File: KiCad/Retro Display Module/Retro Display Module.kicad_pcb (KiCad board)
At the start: 2 copper layers, 70 x 100 mm, 114 parts, among them J1 Conn_01x04_Pin, J10 Conn_01x02_Pin, J11 Conn_01x02_Pin, J12 VCC, J13 TX, J14 RX, J15 CFG, J16 SEL, J17 GND, J18 Conn_01x04_Pin, J19 Conn_01x04_Pin, J2 VCC, J20 Conn_01x02_Pin, J21 Conn_01x04_Pin, J22 Conn_01x02_Pin, J23 Conn_01x02_Pin, J24 Conn_01x02_Pin, J25 Conn_02x03_Odd_Even, J26 Conn_01x02_Pin, J27 Conn_01x02_Pin, J28 Conn_01x02_Pin, J29 Conn_01x04_Pin, J3 TX, J30 Conn_01x02_Pin, J31 Conn_01x02_Pin, J32 Conn_02x11_Odd_Even, J4 RX, J5 CFG, J6 SEL, J7 GND, J8 Conn_01x02_Pin, J9 Conn_01x02_Pin, U1 TS-1187A-B-A-B, U10 D882_C9634, U11 OP07CDR, U12 D882_C9634, U13 D882_C9634, U14 D882_C9634, U15 D882_C9634, U16 D882_C9634, U17 D882_C9634, U18 D882_C9634, U2 STM32G030C8T6, U3 AO3401A, U4 TPS5430DDAR, U5 XC6206P332MR, U6 2N7002, U7 D882_C9634, U8 D882_C9634, U9 D882_C9634, Y1 Crystal

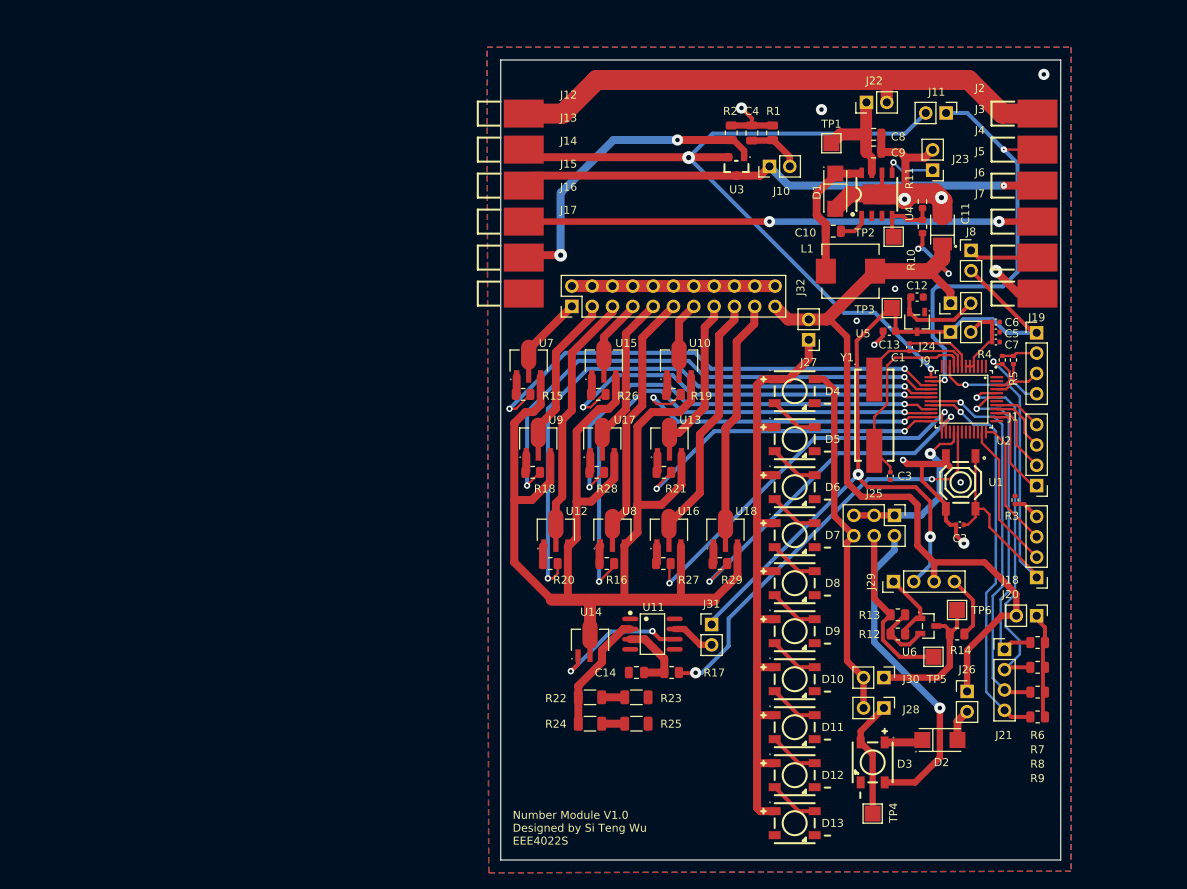
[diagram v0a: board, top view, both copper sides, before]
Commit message: Updated USB PD and Driver LED circuit
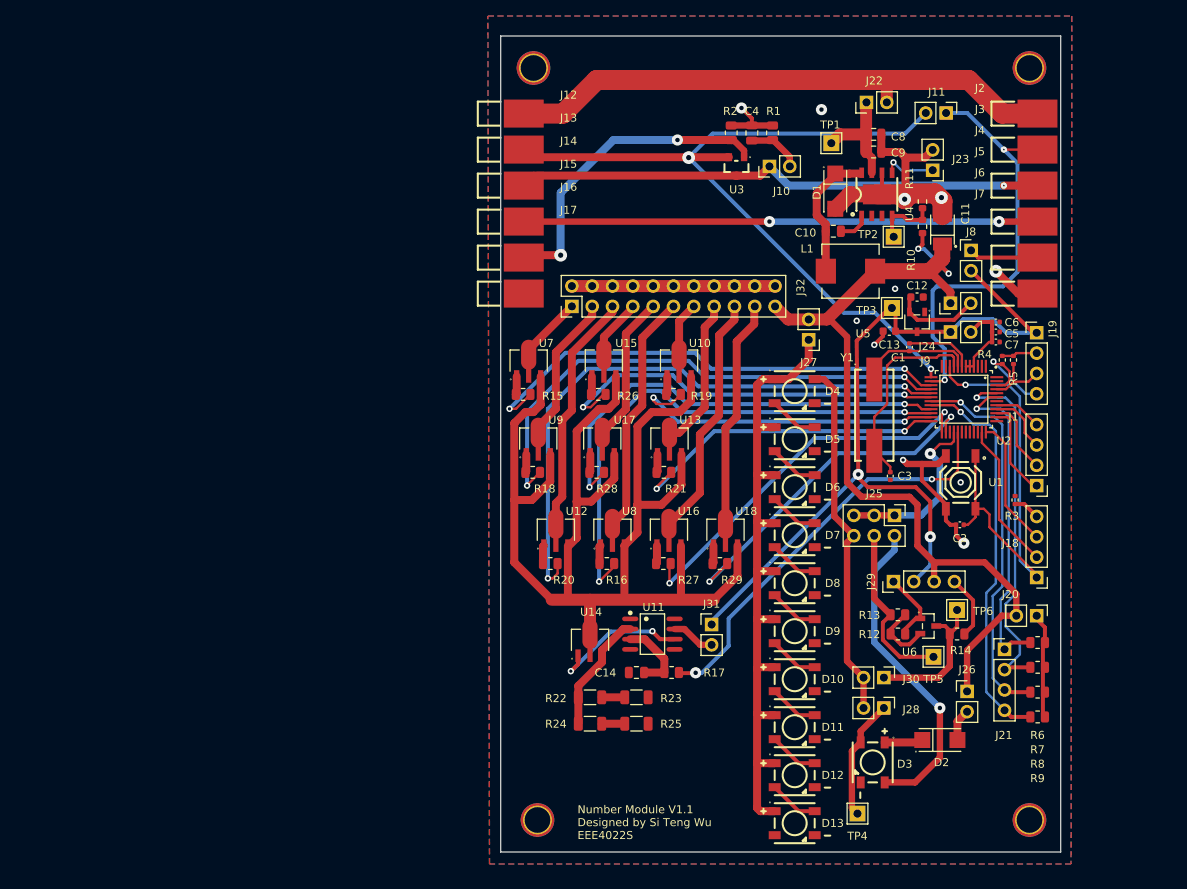
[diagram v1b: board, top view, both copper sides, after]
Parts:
- added H1: M3, Library:MountingHole_3.2mm_M3_Pad_TopBottom, F.Cu at (120.0, 47.0)
- added H2: M3, Library:MountingHole_3.2mm_M3_Pad_TopBottom, F.Cu at (182.0, 47.0)
- added H3: M3, Library:MountingHole_3.2mm_M3_Pad_TopBottom, F.Cu at (120.5, 141.0)
- added H4: M3, Library:MountingHole_3.2mm_M3_Pad_TopBottom, F.Cu at (182.0, 141.0)
- TP1, TP2, TP3, TP4, TP5, TP6: footprint TestPoint:TestPoint_Pad_2.0x2.0mm -> Library:TestPoint_THTPad_2.0x2.0mm_Drill1.0mm
- moved TP4 1.90 mm to (160.5, 140.2)
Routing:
- net GND: track 86.6 -> 85.6 mm, vias 12 -> 11
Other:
- board size 70 x 100 mm -> 70 x 102 mm
- board text added: "Number Module V1.1 Designed by Si Teng Wu EEE4022S"
- board text removed: "Number Module V1.0 Designed by Si Teng Wu EEE4022S"

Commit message: Updated Display PCB
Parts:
- added J33: Conn_01x02_Pin, Connector_PinHeader_2.54mm:PinHeader_1x02_P2.54mm_Vertical, F.Cu at (93.5, 107.2)
- added J34: Conn_02x04_Odd_Even, Connector_PinHeader_2.54mm:PinHeader_2x04_P2.54mm_Vertical, F.Cu at (80.7, 98.9)
- added R30: 100k, Resistor_SMD:R_0402_1005Metric, F.Cu at (85.6, 87.6)
- added R31: 1k, Resistor_SMD:R_0402_1005Metric, F.Cu at (85.6, 89.6)
- added R32: 100k, Resistor_SMD:R_0402_1005Metric, F.Cu at (85.6, 91.6)
- added R33: 1k, Resistor_SMD:R_0402_1005Metric, F.Cu at (85.6, 93.6)
- added R34: 100k, Resistor_SMD:R_0402_1005Metric, F.Cu at (85.6, 95.5)
- added R35: 1k, Resistor_SMD:R_0402_1005Metric, F.Cu at (88.5, 87.6)
- added R36: 100k, Resistor_SMD:R_0402_1005Metric, F.Cu at (88.5, 89.6)
- added R37: 1k, Resistor_SMD:R_0402_1005Metric, F.Cu at (88.5, 91.6)
- added R38: 100k, Resistor_SMD:R_0402_1005Metric, F.Cu at (88.5, 93.6)
- added R39: 1k, Resistor_SMD:R_0402_1005Metric, F.Cu at (88.5, 95.5)
- added R40: 100, Resistor_SMD:R_1206_3216Metric, F.Cu at (88.4, 108.1)
- added R41: 100k, Resistor_SMD:R_0402_1005Metric, F.Cu at (63.6, 101.8)
- added R42: 1k, Resistor_SMD:R_0402_1005Metric, F.Cu at (63.6, 103.8)
- added R43: 100k, Resistor_SMD:R_0402_1005Metric, F.Cu at (63.6, 105.7)
- added R44: 1k, Resistor_SMD:R_0402_1005Metric, F.Cu at (63.6, 107.7)
- added TP7: TestPoint, Library:TestPoint_THTPad_2.0x2.0mm_Drill1.0mm, F.Cu at (80.4, 110.8)
- added U19: AO3401A, Library:SOT-23_L2.9-W1.3-P1.90-LS2.4-BR, F.Cu at (57.1, 88.7)
- added U20: AO3401A, Library:SOT-23_L2.9-W1.3-P1.90-LS2.4-BR, F.Cu at (57.1, 93.4)
- added U21: AO3401A, Library:SOT-23_L2.9-W1.3-P1.90-LS2.4-BR, F.Cu at (57.1, 98.2)
- C14: value 22uF -> 0.1uF; footprint Capacitor_SMD:C_0805_2012Metric -> Capacitor_SMD:C_0402_1005Metric
- C4: value 1nF -> 1uF; footprint Capacitor_SMD:C_0805_2012Metric -> Capacitor_SMD:C_0603_1608Metric
- J1: value Conn_01x04_Pin -> Conn_02x04_Odd_Even; footprint Connector_PinHeader_2.54mm:PinHeader_1x04_P2.54mm_Vertical -> Connector_PinHeader_2.54mm:PinHeader_2x04_P2.54mm_Vertical
- J18, J19: value Conn_01x04_Pin -> Conn_02x03_Odd_Even; footprint Connector_PinHeader_2.54mm:PinHeader_1x04_P2.54mm_Vertical -> Connector_PinHeader_2.54mm:PinHeader_2x03_P2.54mm_Vertical
- J31: value Conn_01x02_Pin -> Conn_01x12_Pin; footprint Connector_PinHeader_2.54mm:PinHeader_1x02_P2.54mm_Vertical -> Connector_PinHeader_2.54mm:PinHeader_1x12_P2.54mm_Vertical
- J32: footprint Connector_PinHeader_2.54mm:PinHeader_2x11_P2.54mm_Vertical -> Connector_PinHeader_2.54mm:PinHeader_2x10_P2.54mm_Vertical
- R1: value 4.7k -> 1k
- R15, R18, R20, R26, R28: value 470 -> 100k; footprint Resistor_SMD:R_0805_2012Metric -> Resistor_SMD:R_0402_1005Metric
- R16, R19, R21, R27, R29: value 470 -> 1k; footprint Resistor_SMD:R_0805_2012Metric -> Resistor_SMD:R_0402_1005Metric
- R22, R23, R24, R25: value 10 -> 100
- U10, U12, U13, U15, U16, U17, U7, U8, U9: value D882_C9634 -> AO3401A; footprint Library:D882 -> Library:SOT-23_L2.9-W1.3-P1.90-LS2.4-BR
- U11: value OP07CDR -> AO3401A; footprint Library:SOIC-8_L4.9-W3.9-P1.27-LS6.0-BL -> Library:SOT-23_L2.9-W1.3-P1.90-LS2.4-BR
- U18: value D882_C9634 -> LM358DR2G; footprint Library:D882 -> Library:Dual LM358
- moved J18 125.9 mm to (57.2, 103.1), turned to 0 degrees
- moved J1 121.3 mm to (62.0, 88.9), turned to 0 degrees
- moved J10 106.6 mm to (57.2, 112.8), turned to 0 degrees
- moved R1 104.9 mm to (61.8, 111.9), turned to 0 degrees
- moved J19 91.0 mm to (92.3, 88.9)
- moved C4 81.8 mm to (87.6, 111.0), turned to 0 degrees
- moved U10 69.7 mm to (71.0, 102.9), turned to 0 degrees
- moved U11 64.7 mm to (71.0, 107.6), turned to 0 degrees
- moved R29 62.0 mm to (82.7, 95.5)
- moved U13 61.2 mm to (75.8, 93.4), turned to 0 degrees
- moved U16 61.2 mm to (75.8, 102.9), turned to 0 degrees
- moved U8 60.0 mm to (71.0, 93.4), turned to 0 degrees
- moved R19 58.0 mm to (79.8, 93.6)
- moved R27 56.3 mm to (82.7, 91.6)
- moved U15 54.8 mm to (75.8, 98.2), turned to 0 degrees
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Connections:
- C14 pad 1: Net-(U11-IN+) -> Net-(J34-Pin_1)
- C4 pad 1: Net-(J10-Pin_2) -> Net-(J19-Pin_5)
- J1 pad 1: Net-(J1-Pin_1) -> /PC6
- J1 pad 3: Net-(J1-Pin_3) -> /PC7
- J14 pad 1: Net-(J10-Pin_1) -> Net-(J14-Pin_1)
- J18 pad 1: /NRST -> /5V
- J18 pad 2: Net-(J18-Pin_2) -> /5V
- J18 pad 3: Net-(J18-Pin_3) -> /3V3
- J18 pad 4: Net-(J18-Pin_4) -> /3V3
- J19 pad 1: /3V3 -> /LED Driver/1OUT
- J19 pad 3: /I2C1_SCL -> /LED Driver/-ve
- J19 pad 4: /I2C1_SDA -> Net-(J19-Pin_4)
- J31 pad 2: Net-(J31-Pin_2) -> /I2C_PUR
- J32 pad 10: Net-(J32-Pin_10) -> /LED Driver/main_col
- J32 pad 12: Net-(J32-Pin_10) -> /LED Driver/main_col
- J32 pad 14: Net-(J32-Pin_10) -> /LED Driver/main_col
- J32 pad 16: Net-(J32-Pin_10) -> /LED Driver/main_col
- J32 pad 18: Net-(J32-Pin_10) -> /LED Driver/main_col
- J32 pad 2: Net-(J32-Pin_10) -> /LED Driver/main_col
- J32 pad 20: Net-(J32-Pin_10) -> /LED Driver/main_col
- J32 pad 4: Net-(J32-Pin_10) -> /LED Driver/main_col
- J32 pad 6: Net-(J32-Pin_10) -> /LED Driver/main_col
- J32 pad 8: Net-(J32-Pin_10) -> /LED Driver/main_col
- J4 pad 1: Net-(J10-Pin_1) -> Net-(J14-Pin_1)
- R15 pad 1: Net-(U7-B) -> /5V
- R15 pad 2: /PA4 -> Net-(U8-G)
- R16 pad 1: Net-(U8-B) -> Net-(U8-G)
- R16 pad 2: /PB10 -> /PA5
- R17 pad 1: Net-(U11-IN+) -> Net-(J19-Pin_5)
- R18 pad 1: Net-(U9-B) -> /5V
- R18 pad 2: /PA5 -> Net-(U9-G)
- R19 pad 1: Net-(U10-B) -> Net-(U9-G)
- R19 pad 2: /PB11 -> /PA6
- R20 pad 1: Net-(U12-B) -> /5V
- R20 pad 2: /PA6 -> Net-(U10-G)
- R21 pad 1: Net-(U13-B) -> Net-(U10-G)
- R21 pad 2: /PB12 -> /PA7
- R22 pad 2: Net-(R22-Pad2) -> GND
- R23 pad 1: Net-(R22-Pad2) -> /LED Driver/-ve
- R24 pad 2: Net-(R24-Pad2) -> GND
- R25 pad 1: Net-(R24-Pad2) -> /LED Driver/-ve
- R26 pad 1: Net-(U15-B) -> /5V
- R26 pad 2: /PA7 -> Net-(U11-G)
- R27 pad 1: Net-(U16-B) -> Net-(U11-G)
- R27 pad 2: /PB13 -> /PB2
- R28 pad 1: Net-(U17-B) -> /5V
- R28 pad 2: /PB2 -> Net-(U12-G)
- R29 pad 1: Net-(U18-B) -> Net-(U12-G)
- R29 pad 2: /PB14 -> /PB10
- R3 pad 2: Net-(J18-Pin_4) -> Net-(J31-Pin_9)
- R4 pad 1: Net-(J19-Pin_2) -> /I2C_PUR
- R5 pad 1: Net-(J19-Pin_2) -> /I2C_PUR
- U10 pad 1: Net-(U10-B) -> Net-(U10-G)
- U10 pad 2: /LED Driver/LED7 -> /5V
- U10 pad 3: /LED Driver/main_col -> /LED Driver/LED4
- U11 pad 1: unconnected-(U11-OFFSET_N1-Pad1) -> Net-(U11-G)
- U11 pad 2: /LED Driver/-ve -> /5V
- U11 pad 3: Net-(U11-IN+) -> /LED Driver/LED5
- U12 pad 1: Net-(U12-B) -> Net-(U12-G)
- U12 pad 2: /LED Driver/LED3 -> /5V
- U12 pad 3: /LED Driver/main_col -> /LED Driver/LED6
- U13 pad 1: Net-(U13-B) -> Net-(U13-G)
- U13 pad 2: /LED Driver/LED8 -> /5V
- U13 pad 3: /LED Driver/main_col -> /LED Driver/LED7
- U14 pad 1: Net-(U11-OUT) -> /LED Driver/1OUT
- U15 pad 1: Net-(U15-B) -> Net-(U15-G)
- U15 pad 2: /LED Driver/LED4 -> /5V
- U15 pad 3: /LED Driver/main_col -> /LED Driver/LED8
- U16 pad 1: Net-(U16-B) -> Net-(U16-G)
- U16 pad 2: /LED Driver/LED9 -> /5V
- U16 pad 3: /LED Driver/main_col -> /LED Driver/LED9
- U17 pad 1: Net-(U17-B) -> Net-(U17-G)
- U17 pad 2: /LED Driver/LED5 -> /5V
- U17 pad 3: /LED Driver/main_col -> /LED Driver/LED0
- U18 pad 1: Net-(U18-B) -> Net-(J19-Pin_2)
- U18 pad 2: /LED Driver/LED0 -> Net-(J19-Pin_4)
- U18 pad 3: /LED Driver/main_col -> Net-(J19-Pin_6)
- U2 pad 30: unconnected-(U2-PC6-Pad30) -> Net-(J1-Pin_2)
- U2 pad 31: unconnected-(U2-PC7-Pad31) -> Net-(J1-Pin_4)
- U2 pad 35: Net-(J18-Pin_2) -> /SWDIO
- U2 pad 36: Net-(J18-Pin_3) -> /SWDCLK/BOOT
- U2 pad 38: Net-(J1-Pin_1) -> /PDO
- U2 pad 39: Net-(J1-Pin_2) -> /PD1
- U2 pad 40: Net-(J1-Pin_3) -> /PD2
- U2 pad 41: Net-(J1-Pin_4) -> /PD3
- U2 pad 47: /PB8 -> unconnected-(U2-PB8-Pad47)
- U2 pad 48: /PB9 -> unconnected-(U2-PB9-Pad48)
- U7 pad 1: Net-(U7-B) -> Net-(U7-G)
- U7 pad 2: /LED Driver/LED1 -> /5V
- U7 pad 3: /LED Driver/main_col -> /LED Driver/LED1
- U8 pad 1: Net-(U8-B) -> Net-(U8-G)
- U8 pad 2: /LED Driver/LED6 -> /5V
- U8 pad 3: /LED Driver/main_col -> /LED Driver/LED2
- U9 pad 1: Net-(U9-B) -> Net-(U9-G)
- U9 pad 2: /LED Driver/LED2 -> /5V
- U9 pad 3: /LED Driver/main_col -> /LED Driver/LED3
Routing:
- net Net-(J10-Pin_1): track 65.8 -> 31.3 mm, vias 1 -> 0
- net Net-(J14-Pin_1): track 0.00 -> 34.5 mm, vias 0 -> 1
- net (no net): track 0.00 -> 31.2 mm
- net /LED Driver/main_col: track 163.3 -> 188.7 mm
- net Net-(J32-Pin_10): track 25.4 -> 0.00 mm
- net /SWDCLK/BOOT: track 0.00 -> 18.5 mm
- net Net-(J18-Pin_2): track 18.5 -> 0.00 mm
- net /SWDIO: track 0.00 -> 18.5 mm
- net Net-(U11-OUT): track 17.8 -> 0.00 mm, vias 2 -> 0
- net /LED Driver/1OUT: track 0.00 -> 17.8 mm, vias 0 -> 2
- net Net-(J18-Pin_3): track 16.3 -> 0.00 mm
- net Net-(J1-Pin_1): track 11.7 -> 0.00 mm
- net /PDO: track 0.00 -> 10.2 mm
- net Net-(U11-IN+): track 9.53 -> 0.00 mm
- net Net-(J19-Pin_5): track 0.00 -> 9.53 mm
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
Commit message: Updated Display PCB
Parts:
- removed the U14 at (127.1, 119.1)
- added U17: MJD44H11J, Library:MJD44 NPN, F.Cu at (124.2, 112.8)
- C1, C14, C2, C3: footprint Capacitor_SMD:C_0402_1005Metric -> Library:C_0402_1005Metric
- C4: renamed from C5; footprint Capacitor_SMD:C_0402_1005Metric -> Library:C_0402_1005Metric
- C5: renamed from C6; footprint Capacitor_SMD:C_0402_1005Metric -> Library:C_0402_1005Metric
- C6: renamed from C7; footprint Capacitor_SMD:C_0402_1005Metric -> Library:C_0402_1005Metric
- R1: renamed from R41; footprint Resistor_SMD:R_0402_1005Metric -> Library:R_0402_1005Metric
- R2: renamed from R42; footprint Resistor_SMD:R_0402_1005Metric -> Library:R_0402_1005Metric
- R20: renamed from R30; footprint Resistor_SMD:R_0402_1005Metric -> Library:R_0402_1005Metric
- R21: renamed from R31; footprint Resistor_SMD:R_0402_1005Metric -> Library:R_0402_1005Metric
- R22: renamed from R28; footprint Resistor_SMD:R_0402_1005Metric -> Library:R_0402_1005Metric
- R23: renamed from R29; footprint Resistor_SMD:R_0402_1005Metric -> Library:R_0402_1005Metric
- R24: renamed from R15; footprint Resistor_SMD:R_0402_1005Metric -> Library:R_0402_1005Metric
- R25: renamed from R16; footprint Resistor_SMD:R_0402_1005Metric -> Library:R_0402_1005Metric
- R26: renamed from R32; footprint Resistor_SMD:R_0402_1005Metric -> Library:R_0402_1005Metric
- R27: renamed from R33; footprint Resistor_SMD:R_0402_1005Metric -> Library:R_0402_1005Metric
- R29: renamed from R18; footprint Resistor_SMD:R_0402_1005Metric -> Library:R_0402_1005Metric
- R3: renamed from R44; footprint Resistor_SMD:R_0402_1005Metric -> Library:R_0402_1005Metric
- R30: renamed from R19; footprint Resistor_SMD:R_0402_1005Metric -> Library:R_0402_1005Metric
- R31: renamed from R34; footprint Resistor_SMD:R_0402_1005Metric -> Library:R_0402_1005Metric
- R32: renamed from R35; footprint Resistor_SMD:R_0402_1005Metric -> Library:R_0402_1005Metric
- R37: renamed from R20; footprint Resistor_SMD:R_0402_1005Metric -> Library:R_0402_1005Metric
- R38: renamed from R21; footprint Resistor_SMD:R_0402_1005Metric -> Library:R_0402_1005Metric
- R39: renamed from R36; footprint Resistor_SMD:R_0402_1005Metric -> Library:R_0402_1005Metric
- R4: renamed from R43; footprint Resistor_SMD:R_0402_1005Metric -> Library:R_0402_1005Metric
- R40: renamed from R37; footprint Resistor_SMD:R_0402_1005Metric -> Library:R_0402_1005Metric
- R41: renamed from R26; footprint Resistor_SMD:R_0402_1005Metric -> Library:R_0402_1005Metric
- R42: renamed from R27; footprint Resistor_SMD:R_0402_1005Metric -> Library:R_0402_1005Metric
- R43: renamed from R38; footprint Resistor_SMD:R_0402_1005Metric -> Library:R_0402_1005Metric
- R44: renamed from R39; footprint Resistor_SMD:R_0402_1005Metric -> Library:R_0402_1005Metric
- R7: renamed from R4; footprint Resistor_SMD:R_0402_1005Metric -> Library:R_0402_1005Metric
- R8: renamed from R5; footprint Resistor_SMD:R_0402_1005Metric -> Library:R_0402_1005Metric
- R9: renamed from R3; footprint Resistor_SMD:R_0402_1005Metric -> Library:R_0402_1005Metric
- moved J1 127.4 mm to (181.8, 132.2), turned to -90 degrees
- moved U2 125.2 mm to (175.0, 140.3), turned to 180 degrees
- moved U1 118.7 mm to (166.2, 140.3), turned to 180 degrees
- moved R4 114.5 mm to (172.4, 141.4), turned to 90 degrees
- moved R3 113.2 mm to (172.4, 138.8), turned to 90 degrees
- moved R1 107.6 mm to (163.6, 141.4), turned to 90 degrees
- moved J10 106.4 mm to (146.4, 54.8), turned to -90 degrees
- moved R2 106.0 mm to (163.6, 138.8), turned to 90 degrees
- moved R5 102.1 mm to (144.0, 51.4)
- moved U4 95.0 mm to (147.3, 59.0), turned to 180 degrees
- moved J19 87.0 mm to (138.9, 72.9), turned to 90 degrees
- moved U21 67.4 mm to (142.2, 96.8), turned to 90 degrees
- moved U19 65.5 mm to (139.8, 88.8), turned to 90 degrees
- moved J12 64.2 mm to (183.0, 52.7)
- moved J13 64.2 mm to (183.0, 57.2)
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- renumbered C11 to C10, C12 to C11, C13 to C12, C4 to C13, C8 to C7, C9 to C8, C10 to C9, J31 to J18, J18 to J19, J19 to J31, J33 to J32, J34 to J33, J32 to J34, R6 to R10, R7 to R11, R8 to R12, R9 to R13, R10 to R14, R11 to R15, R12 to R16, R13 to R17, R14 to R18, R17 to R19, R22 to R28, R23 to R33, R24 to R34, R25 to R35, R40 to R36, R1 to R5, R2 to R6, U20 to U1, U7 to U10, U12 to U11, U18 to U12, U8 to U13, U13 to U14, U9 to U15, U15 to U16, U10 to U18, U16 to U19, U21 to U2, U11 to U20, U17 to U21, U1 to U3, U19 to U4, U2 to U5, U3 to U6, U4 to U7, U5 to U8, U6 to U9
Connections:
- C13 pad 1: Net-(J19-Pin_5) -> Net-(J31-Pin_1)
- J1 pad 1: /PC6 -> GND
- J1 pad 3: /PC7 -> Net-(J1-Pin_3)
- J1 pad 4: Net-(J1-Pin_4) -> /PC7
- J1 pad 5: Net-(J1-Pin_5) -> GND
- J1 pad 6: GND -> Net-(J1-Pin_6)
- J1 pad 8: GND -> /PC6
- J15 pad 1: Net-(J15-Pin_1) -> /PA1
- J18 pad 10: /SWDCLK/BOOT -> /SWDIO
- J18 pad 11: /SWDIO -> /NRST
- J18 pad 12: /NRST -> Net-(J18-Pin_12)
- J18 pad 9: Net-(J31-Pin_9) -> /SWDCLK/BOOT
- J31 pad 1: /LED Driver/1OUT -> Net-(J31-Pin_1)
- J31 pad 2: Net-(J19-Pin_2) -> Net-(J31-Pin_2)
- J31 pad 5: Net-(J19-Pin_5) -> /LED Driver/1OUT
- J31 pad 6: Net-(J19-Pin_6) -> Net-(J31-Pin_6)
- J32 pad 2: /5V -> /LED Driver/5V_PWR
- J34 pad 1: /LED Driver/LED1 -> /LED Driver/LED0
- J34 pad 11: /LED Driver/LED6 -> /LED Driver/LED5
- J34 pad 13: /LED Driver/LED7 -> /LED Driver/LED4
- J34 pad 15: /LED Driver/LED8 -> /LED Driver/LED3
- J34 pad 17: /LED Driver/LED9 -> /LED Driver/LED2
- J34 pad 19: /LED Driver/LED0 -> /LED Driver/LED1
- J34 pad 3: /LED Driver/LED2 -> /LED Driver/LED9
- J34 pad 5: /LED Driver/LED3 -> /LED Driver/LED8
- J34 pad 7: /LED Driver/LED4 -> /LED Driver/LED7
- J34 pad 9: /LED Driver/LED5 -> /LED Driver/LED6
- J5 pad 1: Net-(J15-Pin_1) -> /PA1
- R19 pad 1: Net-(J19-Pin_5) -> Net-(J31-Pin_1)
- R20 pad 1: /5V -> /LED Driver/5V_PWR
- R22 pad 1: /5V -> /LED Driver/5V_PWR
- R23 pad 2: /PB10 -> /PB12
- R24 pad 1: /5V -> /LED Driver/5V_PWR
- R25 pad 2: /PA5 -> /PB10
- R26 pad 1: /5V -> /LED Driver/5V_PWR
- R27 pad 2: /PB11 -> /PA7
- R29 pad 1: /5V -> /LED Driver/5V_PWR
- R30 pad 2: /PA6 -> /PA5
- R31 pad 1: /5V -> /LED Driver/5V_PWR
- R32 pad 2: /PB12 -> /PB13
- R37 pad 1: /5V -> /LED Driver/5V_PWR
- R38 pad 2: /PA7 -> /PB11
- R39 pad 1: /5V -> /LED Driver/5V_PWR
- R40 pad 2: /PB13 -> /PB2
- R41 pad 1: /5V -> /LED Driver/5V_PWR
- R42 pad 2: /PB2 -> /PA6
- R43 pad 1: /5V -> /LED Driver/5V_PWR
- R9 pad 2: Net-(J31-Pin_9) -> Net-(J18-Pin_12)
- U1 pad 3: Net-(J1-Pin_5) -> Net-(J1-Pin_6)
- U10 pad 2: /5V -> /LED Driver/5V_PWR
- U11 pad 2: /5V -> /LED Driver/5V_PWR
- U12 pad 1: Net-(J19-Pin_2) -> Net-(J31-Pin_6)
- U12 pad 3: Net-(J19-Pin_6) -> Net-(J31-Pin_2)
- U13 pad 2: /5V -> /LED Driver/5V_PWR
- U14 pad 2: /5V -> /LED Driver/5V_PWR
- U15 pad 2: /5V -> /LED Driver/5V_PWR
- U16 pad 2: /5V -> /LED Driver/5V_PWR
- U18 pad 2: /5V -> /LED Driver/5V_PWR
- U19 pad 2: /5V -> /LED Driver/5V_PWR
- U2 pad 3: Net-(J1-Pin_7) -> Net-(J1-Pin_2)
- U20 pad 2: /5V -> /LED Driver/5V_PWR
- U21 pad 2: /5V -> /LED Driver/5V_PWR
- U5 pad 12: unconnected-(U2-PA1-Pad12) -> /PA1
- U5 pad 30: Net-(J1-Pin_2) -> Net-(J1-Pin_7)
- U5 pad 31: Net-(J1-Pin_4) -> Net-(J1-Pin_3)
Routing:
- net /LED Driver/main_col: track 188.7 -> 65.4 mm
- net /LED Driver/5V_PWR: track 0.00 -> 109.5 mm
- net /PA1: track 0.00 -> 84.4 mm, vias 0 -> 3
- net /5V: track 110.1 -> 188.7 mm, vias 2 -> 4
- net Net-(J15-Pin_1): track 63.8 -> 0.00 mm, vias 2 -> 0
- net /VCC: track 116.6 -> 72.4 mm
- net Net-(J1-Pin_3): track 0.00 -> 41.8 mm, vias 0 -> 1
- net Net-(J1-Pin_7): track 0.00 -> 41.5 mm, vias 0 -> 1
- net /PA6: track 75.1 -> 40.4 mm
- net Net-(J14-Pin_1): track 34.5 -> 66.0 mm, vias 1 -> 2
- net (no net): track 31.2 -> 0.00 mm
- net /LED Driver/LED6: track 30.4 -> 3.24 mm
- net /PB2: track 56.3 -> 30.2 mm
- net /LED Driver/LED0: track 28.7 -> 3.24 mm
- net /PA5: track 66.1 -> 46.3 mm
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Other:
- outline, holes or cut-outs redrawn
- board text added: "CFG"
- board text added: "GND"
- board text added: "RX"
- board text added: "SEL"
- board text added: "TX"
- board text added: "VCC"

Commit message: Begin STM32 Programming
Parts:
- added D14: XL-1615RGBC-WS2812B, Library:LED-SMD_4P-L1.6-W1.5_XL-1615RGBC-WS2812B, F.Cu at (153.6, 110.0)
- added D15: XL-1615RGBC-WS2812B, Library:LED-SMD_4P-L1.6-W1.5_XL-1615RGBC-WS2812B, F.Cu at (148.8, 110.0)
- added D16: XL-1615RGBC-WS2812B, Library:LED-SMD_4P-L1.6-W1.5_XL-1615RGBC-WS2812B, F.Cu at (153.6, 104.0)
- added D17: XL-1615RGBC-WS2812B, Library:LED-SMD_4P-L1.6-W1.5_XL-1615RGBC-WS2812B, F.Cu at (148.8, 104.0)
- added D18: XL-1615RGBC-WS2812B, Library:LED-SMD_4P-L1.6-W1.5_XL-1615RGBC-WS2812B, F.Cu at (153.6, 98.0)
- added D19: XL-1615RGBC-WS2812B, Library:LED-SMD_4P-L1.6-W1.5_XL-1615RGBC-WS2812B, F.Cu at (148.8, 98.0)
- added D20: XL-1615RGBC-WS2812B, Library:LED-SMD_4P-L1.6-W1.5_XL-1615RGBC-WS2812B, F.Cu at (153.6, 92.0)
- added D21: XL-1615RGBC-WS2812B, Library:LED-SMD_4P-L1.6-W1.5_XL-1615RGBC-WS2812B, F.Cu at (148.8, 92.0)
- added D22: XL-1615RGBC-WS2812B, Library:LED-SMD_4P-L1.6-W1.5_XL-1615RGBC-WS2812B, F.Cu at (153.6, 86.0)
- added D23: XL-1615RGBC-WS2812B, Library:LED-SMD_4P-L1.6-W1.5_XL-1615RGBC-WS2812B, F.Cu at (148.8, 86.0)
- added JP1: Jumper_2_Open, Jumper:SolderJumper-2_P1.3mm_Open_RoundedPad1.0x1.5mm, F.Cu at (136.2, 116.1)
- added R41: 100, Resistor_SMD:R_1206_3216Metric, F.Cu at (142.3, 120.4)
- added R42: 100, Resistor_SMD:R_1206_3216Metric, F.Cu at (139.3, 120.4)
- added R47: 100, Resistor_SMD:R_1206_3216Metric, F.Cu at (136.2, 120.4)
- added R48: 100, Resistor_SMD:R_1206_3216Metric, F.Cu at (133.1, 120.4)
- added R49: 100, Resistor_SMD:R_1206_3216Metric, F.Cu at (130.1, 120.4)
- D10, D11, D12, D13, D3, D4, D5, D6, D7, D8, D9: value WS2812B -> XL-1615RGBC-WS2812B; footprint Library:LED-SMD_4P-L5.0-W5.0-BL_XL-5050RGBC -> Library:LED-SMD_4P-L1.6-W1.5_XL-1615RGBC-WS2812B
- R1, R2, R20, R21, R22, R23, R24, R25, R26, R27, R29, R3, R30, R31, R32, R37, R38, R39, R4, R40, R7, R8, R9: footprint Library:R_0402_1005Metric -> Library:R_0402_1005Metric_Pad0.72x0.64mm_HandSolder
- R43: renamed from R41; footprint Library:R_0402_1005Metric -> Library:R_0402_1005Metric_Pad0.72x0.64mm_HandSolder
- R44: renamed from R42; footprint Library:R_0402_1005Metric -> Library:R_0402_1005Metric_Pad0.72x0.64mm_HandSolder
- R45: renamed from R43; footprint Library:R_0402_1005Metric -> Library:R_0402_1005Metric_Pad0.72x0.64mm_HandSolder
- R46: renamed from R44; footprint Library:R_0402_1005Metric -> Library:R_0402_1005Metric_Pad0.72x0.64mm_HandSolder
- R6: value 4.7k -> 100k; footprint Resistor_SMD:R_0805_2012Metric -> Library:R_0402_1005Metric_Pad0.72x0.64mm_HandSolder
- moved D4 52.7 mm to (148.8, 140.0)
- moved D5 41.8 mm to (166.4, 132.9), turned to 0 degrees
- moved D6 34.6 mm to (153.6, 134.0)
- moved D7 28.9 mm to (148.8, 134.0)
- moved D13 25.7 mm to (148.8, 116.0)
- moved D12 19.4 mm to (153.6, 116.0)
- moved D8 16.6 mm to (153.6, 128.0)
- moved D3 14.8 mm to (153.6, 140.0)
- moved D9 11.3 mm to (148.8, 128.0)
- moved D11 8.34 mm to (148.8, 122.0)
- moved J33 5.30 mm to (140.0, 127.7)
- moved C13 5.30 mm to (135.8, 124.5)
- moved C14 5.30 mm to (135.2, 130.3)
- moved J31 5.30 mm to (132.2, 126.7)
- moved U12 5.30 mm to (132.4, 134.5)
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- renumbered J26 to J25, J27 to J26, J25 to J27, TP5 to TP4, TP4 to TP5
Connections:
- D10 pad 1: Net-(D10-VDD) -> Net-(D10-DO)
- D10 pad 2: Net-(D10-DOUT) -> Net-(D10-VDD)
- D10 pad 4: Net-(D10-DIN) -> Net-(D10-DI)
- D11 pad 1: Net-(D10-VDD) -> Net-(D11-DO)
- D11 pad 2: Net-(D11-DOUT) -> Net-(D10-VDD)
- D11 pad 4: Net-(D10-DOUT) -> Net-(D11-DI)
- D12 pad 1: Net-(D10-VDD) -> Net-(D12-DO)
- D12 pad 2: Net-(D12-DOUT) -> Net-(D10-VDD)
- D12 pad 4: Net-(D11-DOUT) -> Net-(D10-DO)
- D13 pad 1: Net-(D10-VDD) -> Net-(D13-DO)
- D13 pad 2: unconnected-(D13-DOUT-Pad2) -> Net-(D10-VDD)
- D13 pad 4: Net-(D12-DOUT) -> Net-(D11-DO)
- D3 pad 1: Net-(D2-K) -> Net-(D3-DO)
- D3 pad 2: Net-(D3-DOUT) -> Net-(D10-VDD)
- D3 pad 4: /RGB LEDs/Cheese -> /RGB LEDs/DIN
- D4 pad 1: Net-(D10-VDD) -> Net-(D4-DO)
- D4 pad 2: Net-(D4-DOUT) -> Net-(D10-VDD)
- D5 pad 1: Net-(D10-VDD) -> Net-(D5-DO)
- D5 pad 2: Net-(D5-DOUT) -> Net-(D2-K)
- D5 pad 4: Net-(D4-DOUT) -> /RGB LEDs/Cheese
- D6 pad 1: Net-(D10-VDD) -> Net-(D6-DO)
- D6 pad 2: Net-(D6-DOUT) -> Net-(D10-VDD)
- D6 pad 4: Net-(D5-DOUT) -> Net-(D3-DO)
- D7 pad 1: Net-(D10-VDD) -> Net-(D7-DO)
- D7 pad 2: Net-(D7-DOUT) -> Net-(D10-VDD)
- D7 pad 4: Net-(D6-DOUT) -> Net-(D4-DO)
- D8 pad 1: Net-(D10-VDD) -> Net-(D10-DI)
- D8 pad 2: Net-(D8-DOUT) -> Net-(D10-VDD)
- D8 pad 4: Net-(D7-DOUT) -> Net-(D6-DO)
- D9 pad 1: Net-(D10-VDD) -> Net-(D11-DI)
- D9 pad 2: Net-(D10-DIN) -> Net-(D10-VDD)
- D9 pad 4: Net-(D8-DOUT) -> Net-(D7-DO)
- J28 pad 1: Net-(D3-DOUT) -> Net-(D5-DO)
- TP5 pad 1: Net-(D3-DOUT) -> Net-(D5-DO)
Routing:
- net Net-(D10-VDD): track 83.4 -> 159.4 mm
- net /PA1: track 84.4 -> 141.0 mm
- net Net-(JP1-B): track 0.00 -> 14.5 mm
- net Net-(D3-DOUT): track 10.4 -> 0.00 mm
- net Net-(D5-DO): track 0.00 -> 8.79 mm
- net /LED Driver/-ve: track 28.5 -> 35.4 mm
- net /TIM1_CH2: track 49.1 -> 55.5 mm
- net Net-(D8-DOUT): track 6.24 -> 0.00 mm
- net Net-(D7-DOUT): track 6.24 -> 0.00 mm
- net Net-(D6-DOUT): track 6.24 -> 0.00 mm
- net Net-(D5-DOUT): track 6.24 -> 0.00 mm
- net Net-(D4-DOUT): track 6.24 -> 0.00 mm
- net Net-(D10-DOUT): track 6.24 -> 0.00 mm
- net Net-(D10-DIN): track 6.24 -> 0.00 mm
- net Net-(D12-DOUT): track 6.24 -> 0.00 mm
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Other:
- board size 70 x 102 mm -> 70 x 100 mm
- board text added: "Number Module V1.2 Designed by Si Teng Wu EEE4022S"
- board text removed: "Number Module V1.1 Designed by Si Teng Wu EEE4022S"
